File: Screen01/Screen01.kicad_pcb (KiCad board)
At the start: 2 copper layers, 3 parts, among them J1 Conn_01x03_MountingPin, U1 NodeMCU_Amica_R2, U2 CR2013-MI2120

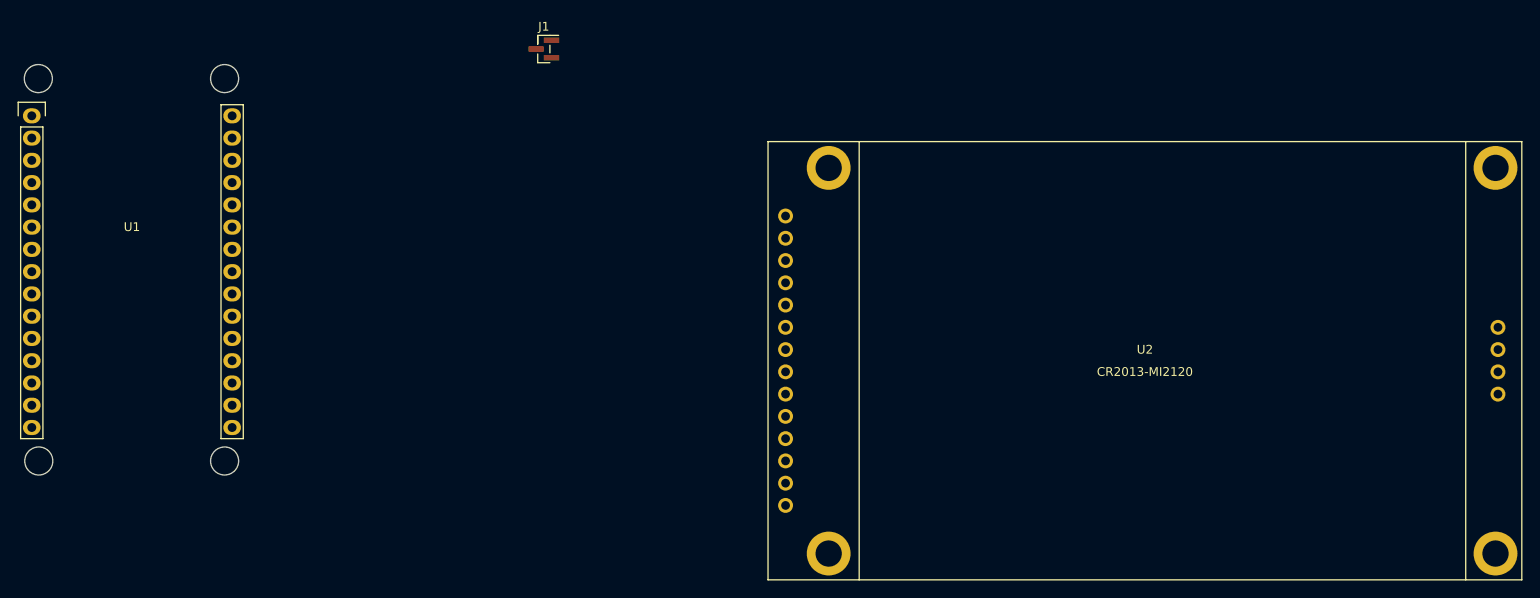
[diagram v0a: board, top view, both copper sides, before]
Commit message: Will use an ultrasonic sensor instead of a PIR
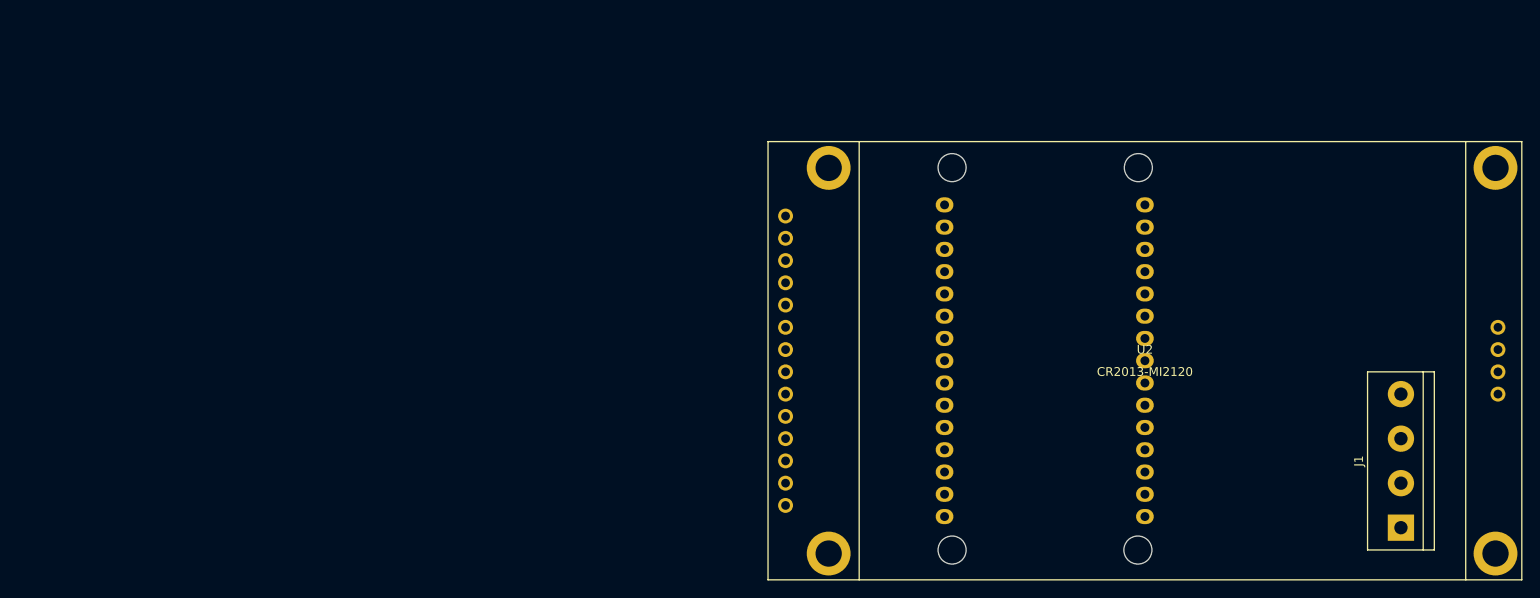
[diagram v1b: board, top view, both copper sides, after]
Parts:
- J1: value Conn_01x03_MountingPin -> UlrSonc; footprint Connector_PinHeader_1.00mm:PinHeader_1x03_P1.00mm_Vertical_SMD_Pin1Right -> TerminalBlock:TerminalBlock_bornier-4_P5.08mm
- U1: value NodeMCU_Amica_R2 -> NodeMCU; moved to B.Cu
- moved U1 127.4 mm to (217.2, 45.7), turned to 180 degrees
- moved J1 112.0 mm to (246.4, 82.5), turned to 90 degrees
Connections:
- J1 pad 2: /PIRDATA -> /TRIG
- J1 pad 3: GND -> /ECHO
- U1 pad 10: Net-(U1-Pad10) -> GND
- U1 pad 24: Net-(U1-Pad24) -> GND
- U1 pad 27: /PIRDATA -> /ECHO
- U1 pad 30: Net-(U1-Pad30) -> /TRIG
